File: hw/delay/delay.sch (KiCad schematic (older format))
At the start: 24 parts, among them J1 conn_trigger, J2 conn_done, J3 FTDI, J4 conn_active, SW1 Rotary_Encoder_Switch, SW2 switch_active, SW3 switch_reset, U1 ATmega328P-PU, U2 LTC-4724JR, Y1 Crystal

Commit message: DELAY block v2
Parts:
- removed J1: conn_trigger, Connector_PinHeader_2.54mm:PinHeader_1x03_P2.54mm_Vertical, symbol Connector:Conn_01x03_Male
- removed J2: conn_done, Connector_PinHeader_2.54mm:PinHeader_1x03_P2.54mm_Vertical, symbol Connector:Conn_01x03_Male
- removed J4: conn_active, Connector_PinHeader_2.54mm:PinHeader_1x03_P2.54mm_Vertical, symbol Connector:Conn_01x03_Male
- removed SW2: switch_active, autoblocks:SW_PUSH_6mm_H5mm, symbol Switch:SW_Push_Dual
- removed SW3: switch_reset, autoblocks:SW_PUSH_6mm_H5mm, symbol Switch:SW_Push_Dual
- removed U1: ATmega328P-PU, Package_DIP:DIP-28_W7.62mm, symbol MCU_Microchip_ATmega:ATmega328P-PU
- added D2: DIODE, Diode_SMD:D_0603_1608Metric, symbol pspice:DIODE
- added H5: led_spy_hole, MountingHole:MountingHole_3.2mm_M3, symbol Mechanical:MountingHole_Pad
- added J1: bootloader, autoblocks:edge_connector_3, symbol Connector:Conn_01x06_Male
- added J5: BUS, Connector_PinHeader_2.54mm:PinHeader_2x07_P2.54mm_Vertical, symbol Connector_Generic:Conn_02x07_Counter_Clockwise
- added R5, R6, R7: 1k, Resistor_SMD:R_0603_1608Metric, symbol Device:R
- added SW2: active, Button_Switch_SMD:SW_SPST_TL3305C, symbol Switch:SW_Push
- added SW3: reset, Button_Switch_SMD:SW_SPST_TL3305C, symbol Switch:SW_Push
- added SW4: NEXT, Package_DIP:DIP-16_W7.62mm_SMDSocket_SmallPads, symbol Switch:SW_DIP_x08
- added SW5: ACTIVE, Package_DIP:DIP-16_W7.62mm_SMDSocket_SmallPads, symbol Switch:SW_DIP_x08
- added SW6: ID, Package_DIP:DIP-16_W7.62mm_SMDSocket_SmallPads, symbol Switch:SW_DIP_x08
- added U1: ATmega328-AU, Package_QFP:TQFP-32_7x7mm_P0.8mm, symbol MCU_Microchip_ATmega:ATmega328-AU
- C1: footprint Capacitor_THT:CP_Radial_Tantal_D6.0mm_P2.50mm -> Capacitor_SMD:C_0603_1608Metric
- C2, C3: footprint Capacitor_THT:C_Disc_D3.0mm_W1.6mm_P2.50mm -> Capacitor_SMD:C_0603_1608Metric
- C4, C5: footprint Capacitor_THT:C_Axial_L5.1mm_D3.1mm_P7.50mm_Horizontal -> Capacitor_SMD:C_0603_1608Metric
- H1, H2, H3, H4: footprint MountingHole:MountingHole_2.2mm_M2 -> MountingHole:MountingHole_3.2mm_M3_Pad
- J3: footprint Connector_PinHeader_2.54mm:PinHeader_1x06_P2.54mm_Vertical -> autoblocks:edge_connector_3
- R1, R2, R3, R4: footprint Resistor_THT:R_Axial_DIN0207_L6.3mm_D2.5mm_P10.16mm_Horizontal -> Resistor_SMD:R_0603_1608Metric
- Y1: footprint Crystal:Crystal_HC18-U_Vertical -> Crystal:Crystal_SMD_HC49-SD
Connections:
- net labels added: bus1, bus10, bus11, bus12, bus13, bus14, bus2, bus3, bus4, bus5, bus6, bus7, bus8, bus9
- wire segments 138 -> 181
- no-connect marks 0 -> 6
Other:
- moved on the sheet: D1, H1, H2, H3, H4, J3, R1, R3, R4, SW1, U2

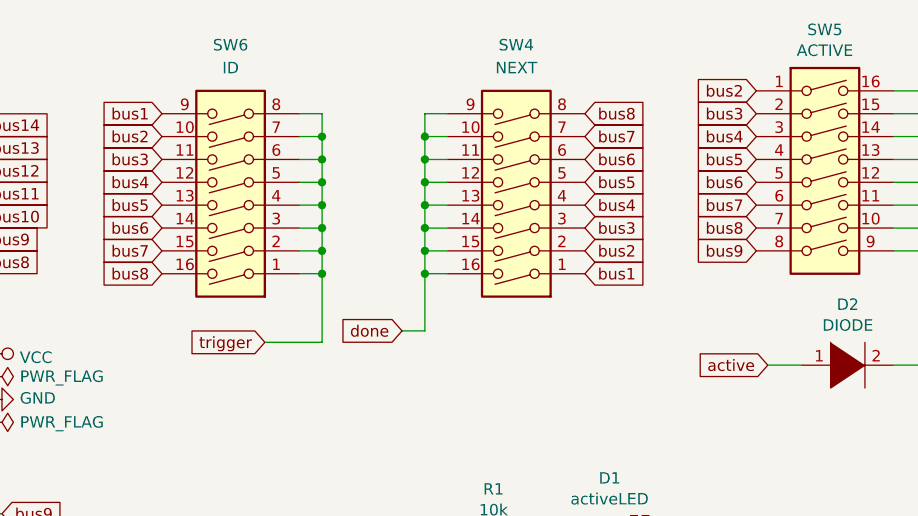
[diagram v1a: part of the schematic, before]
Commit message: fix DELAY bus assigments
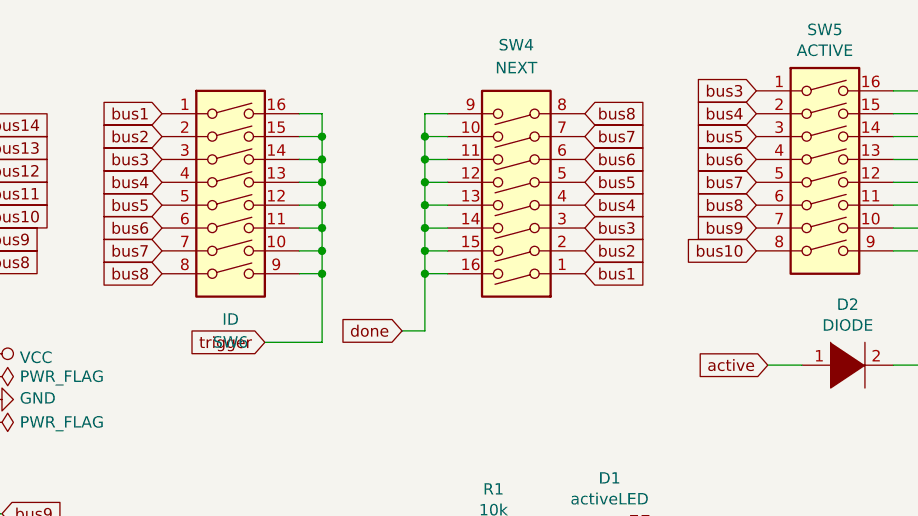
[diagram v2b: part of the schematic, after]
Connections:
- net RX: now also SW5.7; no longer SW5.8
- net TX: now also SW5.8
- net a0: now also SW6.10, SW6.11, SW6.12, SW6.13, SW6.14, SW6.15, SW6.16, SW6.9; no longer SW6.1, SW6.2, SW6.3, SW6.4, SW6.5, SW6.6, SW6.7, SW6.8
- net bus1: now also SW6.1; no longer SW6.9
- net bus2: now also SW6.2; no longer SW5.1, SW6.10
- net bus3: now also SW5.1, SW6.3; no longer SW5.2, SW6.11
- net bus4: now also SW5.2, SW6.4; no longer SW5.3, SW6.12
- net bus5: now also SW5.3, SW6.5; no longer SW5.4, SW6.13
- net bus6: now also SW5.4, SW6.6; no longer SW5.5, SW6.14
- net bus7: now also SW5.5, SW6.7; no longer SW5.6, SW6.15
- net bus8: now also SW5.6, SW6.8; no longer SW5.7, SW6.16
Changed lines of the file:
@@
 $EndComp
 Text GLabel 9850 1100 0    50   Input ~ 0
-bus2
+bus3
 Text GLabel 9850 1200 0    50   Input ~ 0
-bus3
+bus4
 Text GLabel 9850 1300 0    50   Input ~ 0
-bus4
+bus5
 Text GLabel 9850 1400 0    50   Input ~ 0
-bus5
+bus6
 Text GLabel 9850 1500 0    50   Input ~ 0
-bus6
+bus7
 Text GLabel 9850 1600 0    50   Input ~ 0
-bus7
+bus8
 Text GLabel 9850 1700 0    50   Input ~ 0
-bus8
-Text GLabel 9850 1800 0    50   Input ~ 0
 bus9
 Wire Wire Line
@@
 L Switch:SW_DIP_x08 SW6
 U 1 1 5C35B265
-P 7550 1500
-F 0 "SW6" H 7550 900 50  0000 C CNN
-F 1 "ID" H 7550 1000 50  0000 C CNN
-F 2 "Package_DIP:DIP-16_W7.62mm_SMDSocket_SmallPads" H 7550 1500 50  0001 C CNN
-F 3 "" H 7550 1500 50  0001 C CNN
-	1    7550 1500
-	-1   0    0    1
+P 7550 1600
+F 0 "SW6" H 7550 1000 50  0000 C CNN
+F 1 "ID" H 7550 1100 50  0000 C CNN
+F 2 "Package_DIP:DIP-16_W7.62mm_SMDSocket_SmallPads" H 7550 1600 50  0001 C CNN
+F 3 "" H 7550 1600 50  0001 C CNN
+	1    7550 1600
+	1    0    0    -1
 $EndComp
 $Comp
@@
 	0    1    1    0
 $EndComp
+Text GLabel 9850 1800 0    50   Input ~ 0
+bus10
 $EndSCHEMATC
